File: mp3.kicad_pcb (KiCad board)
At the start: 2 copper layers, 58 x 79 mm, 51 parts, among them J1 AudioJack4_Ground, J2 AudioJack4_Ground, J3 Conn_01x08, J4 Micro_SD_Card_Det1, Q1 8205A_C14212, SW2 SW_Nidec_CAS-120A1, U1 XTAD5142IRGER, U2 MCP6002-xSN, U3 DW01A_C351410, U5 TP4056-42-ESOP8

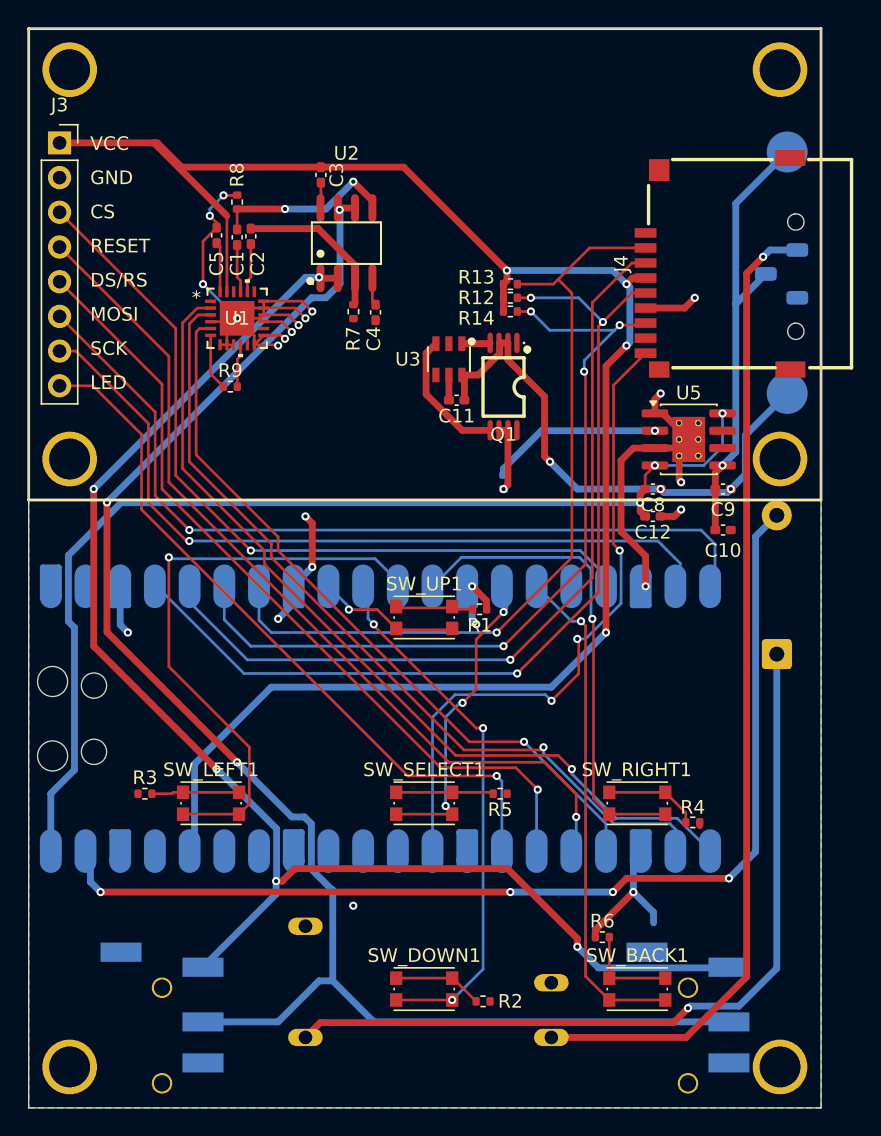
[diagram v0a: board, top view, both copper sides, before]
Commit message: Move microSD card slot and update PCB
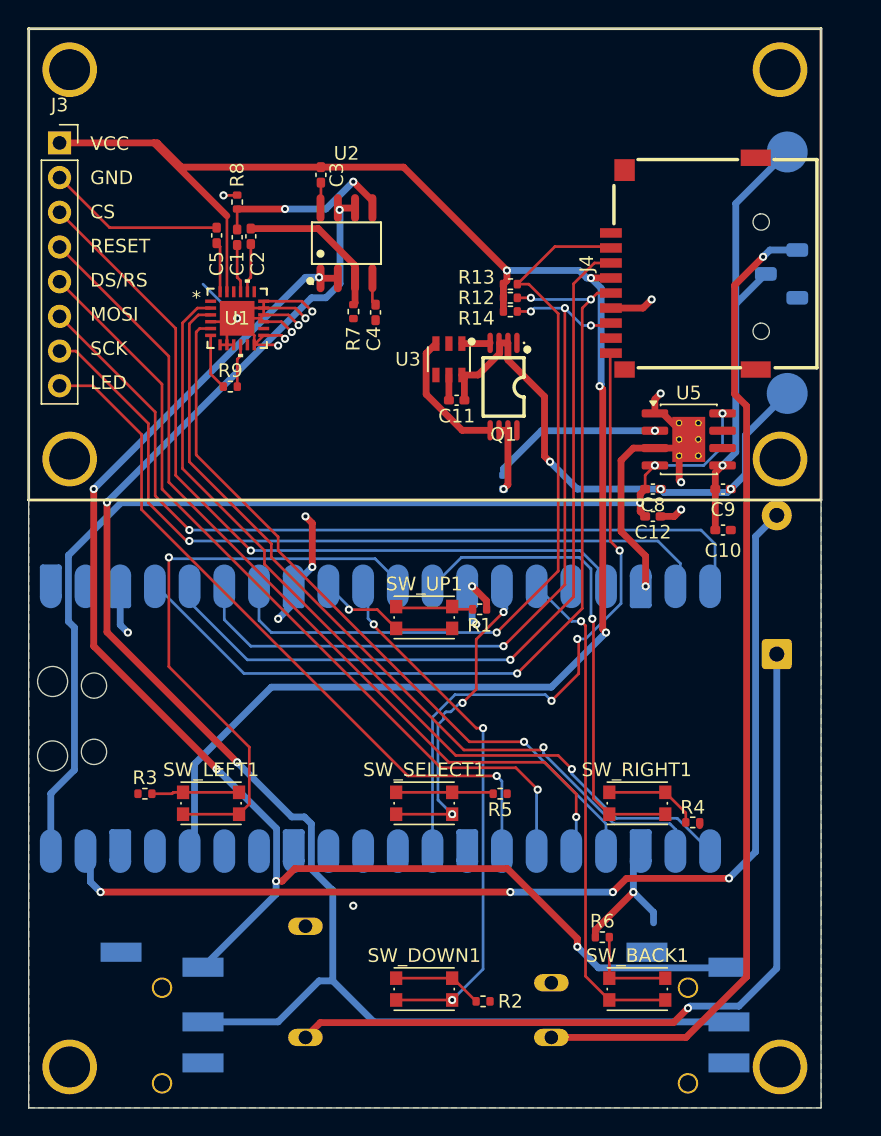
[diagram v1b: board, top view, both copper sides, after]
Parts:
- moved J4 2.54 mm to (119.2, 68.5)
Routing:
- net GND: track 103.8 -> 108.6 mm, vias 24 -> 22
- net /Pico_3V3: track 131.0 -> 127.7 mm
- net /SD_CS: track 60.0 -> 57.4 mm
- net /SD_CLK: track 68.6 -> 65.9 mm
- net /SD_MISO: track 60.4 -> 57.8 mm
- net /SD_MOSI: track 60.1 -> 59.2 mm
- net /SD_DET: track 48.6 -> 47.7 mm
- net /CKCS_IN: track 72.0 -> 72.8 mm
- net /BTN_SELECT: track 23.1 -> 23.7 mm
